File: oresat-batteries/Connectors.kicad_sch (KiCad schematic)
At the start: 13 parts, among them SW1 OMRON-D2F-5L3-LEFT, SW2 OMRON-D2F-5L3-RIGHT, SW3 OMRON-D2F-5L3-LEFT, SW4 OMRON-D2F-5L3-RIGHT

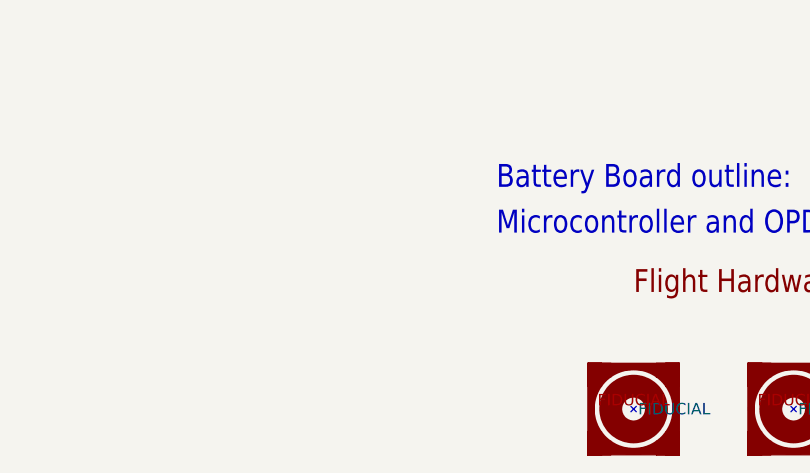
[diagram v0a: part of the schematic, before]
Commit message: Fixed the voltage regulator problem, and the DRC is happy
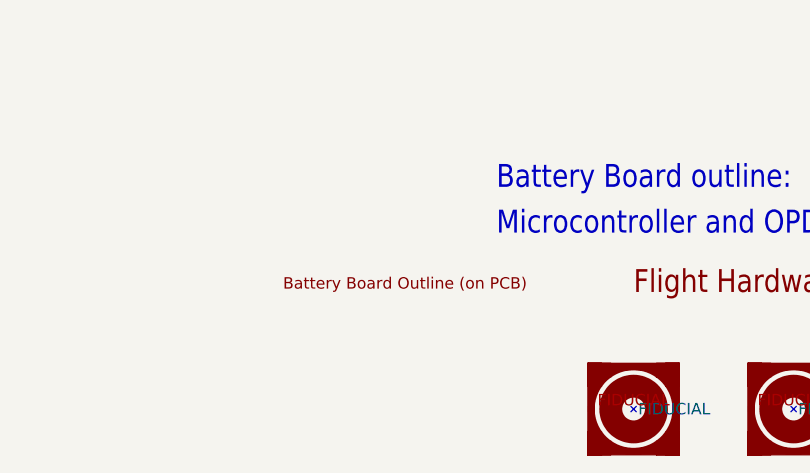
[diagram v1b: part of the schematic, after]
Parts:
- added U$2: BatteryBoardOutline, oresat-footprints:ORESAT-CARD-V1.3-BATTERY-V3.0, symbol OreSat-BatteryBoardOutline:BatteryBoardOutline
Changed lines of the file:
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@@
     (pin "NO")
+  )
+  (symbol (lib_id "OreSat-BatteryBoardOutline:BatteryBoardOutline") (at 336.55 246.38 0) (unit 1)
+    (in_bom yes) (on_board yes) (fields_autoplaced)
+    (property "Reference" "U$2" (id 0) (at 336.55 239.1257 0)
+      (effects (font (size 1.27 1.27)) hide)
+    )
+    (property "Value" "BatteryBoardOutline" (id 1) (at 336.55 241.6626 0)
+      (effects (font (size 1.27 1.27)) hide)
+    )
+    (property "Footprint" "oresat-footprints:ORESAT-CARD-V1.3-BATTERY-V3.0" (id 2) (at 336.55 246.38 0)
+      (effects (font (size 1.27 1.27)) hide)
+    )
+    (property "Datasheet" "" (id 3) (at 336.55 246.38 0)
+      (effects (font (size 1.27 1.27)) hide)
+    )
   )
   (symbol (lib_id "oresat-batteries-eagle-import:GND") (at 184.15 163.83 0) (mirror y) (unit 1)
